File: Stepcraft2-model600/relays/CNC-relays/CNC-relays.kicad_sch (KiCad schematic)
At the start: 43 parts, among them J1 PC-GK2.1, J2 Conn_02x04_Odd_Even, J3 Conn_02x04_Odd_Even, J4 Conn_01x01, J5 FTDI breakout, J6 Conn_01x03, J7 Conn_01x03, J8 Conn_01x03, J9 Conn_01x03, U1 WT32-ETH01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

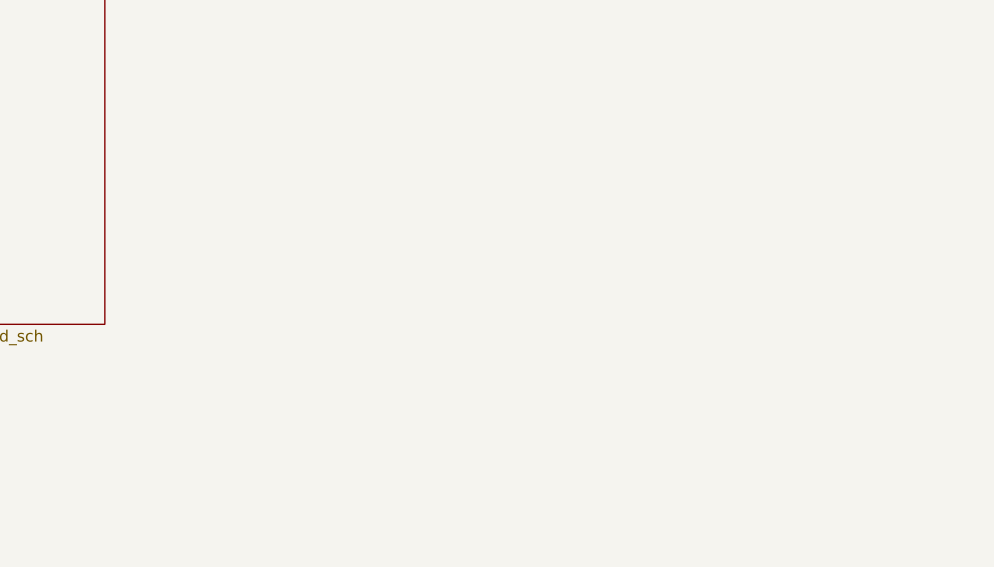
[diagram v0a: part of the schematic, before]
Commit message: Add notes to CNC-relays project
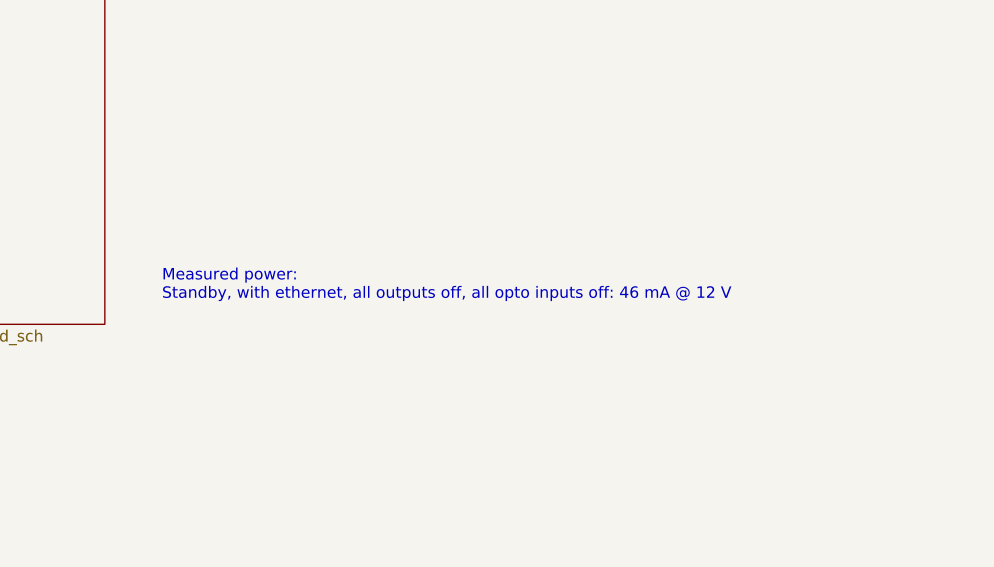
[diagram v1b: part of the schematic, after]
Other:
- note added: "Measured power: Standby, with ethernet, all outputs off, all opto inputs off: 46 mA @ 12 V"
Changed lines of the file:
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@@
+    (effects (font (size 1.27 1.27)) (justify left bottom))
+  )
+  (text "Measured power:\nStandby, with ethernet, all outputs off, all opto inputs off: 46 mA @ 12 V"
+    (at 209.55 157.48 0)
     (effects (font (size 1.27 1.27)) (justify left bottom))
   )
